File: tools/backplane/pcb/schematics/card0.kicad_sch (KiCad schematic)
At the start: 3 parts

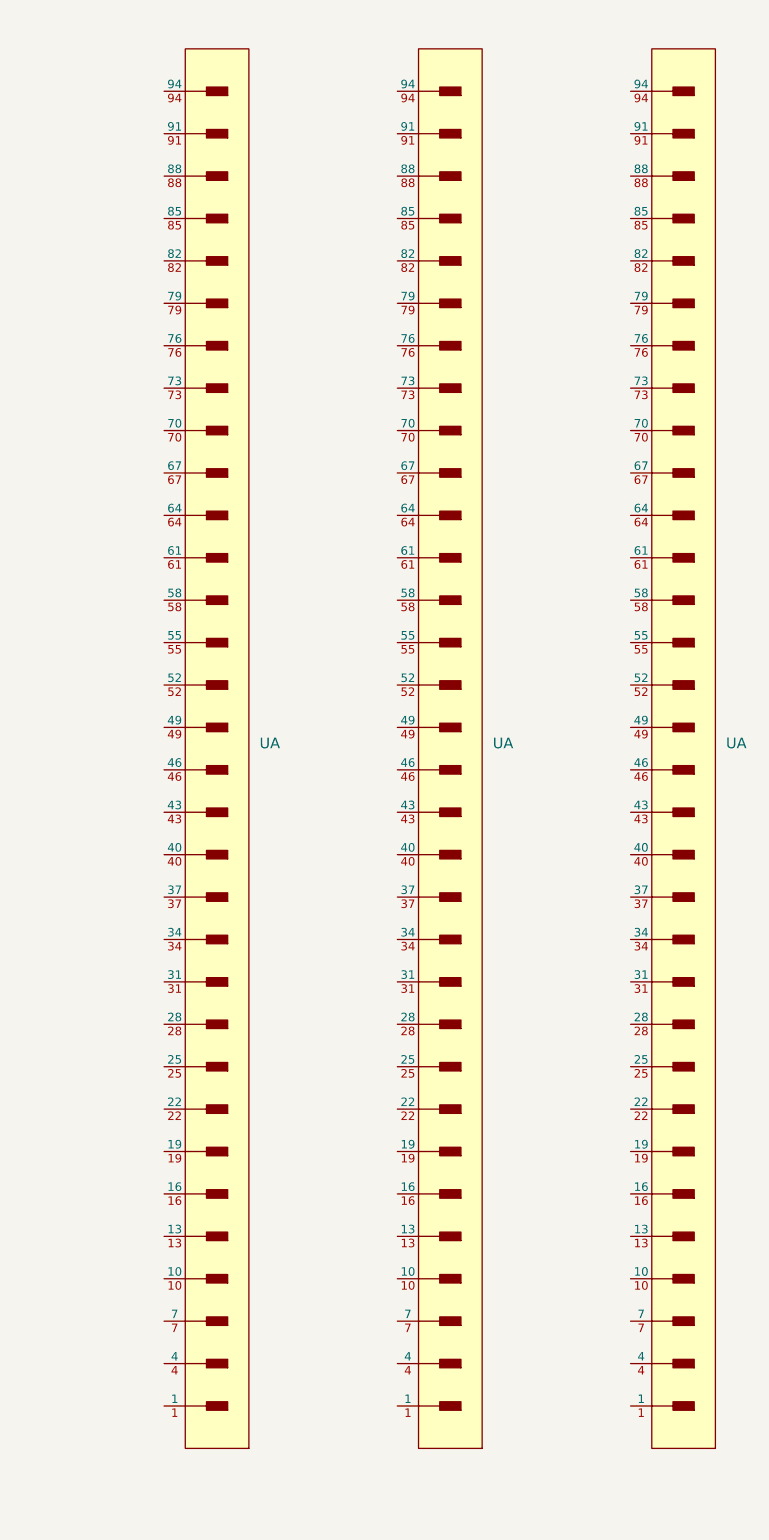
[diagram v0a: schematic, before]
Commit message: start routing the backplane
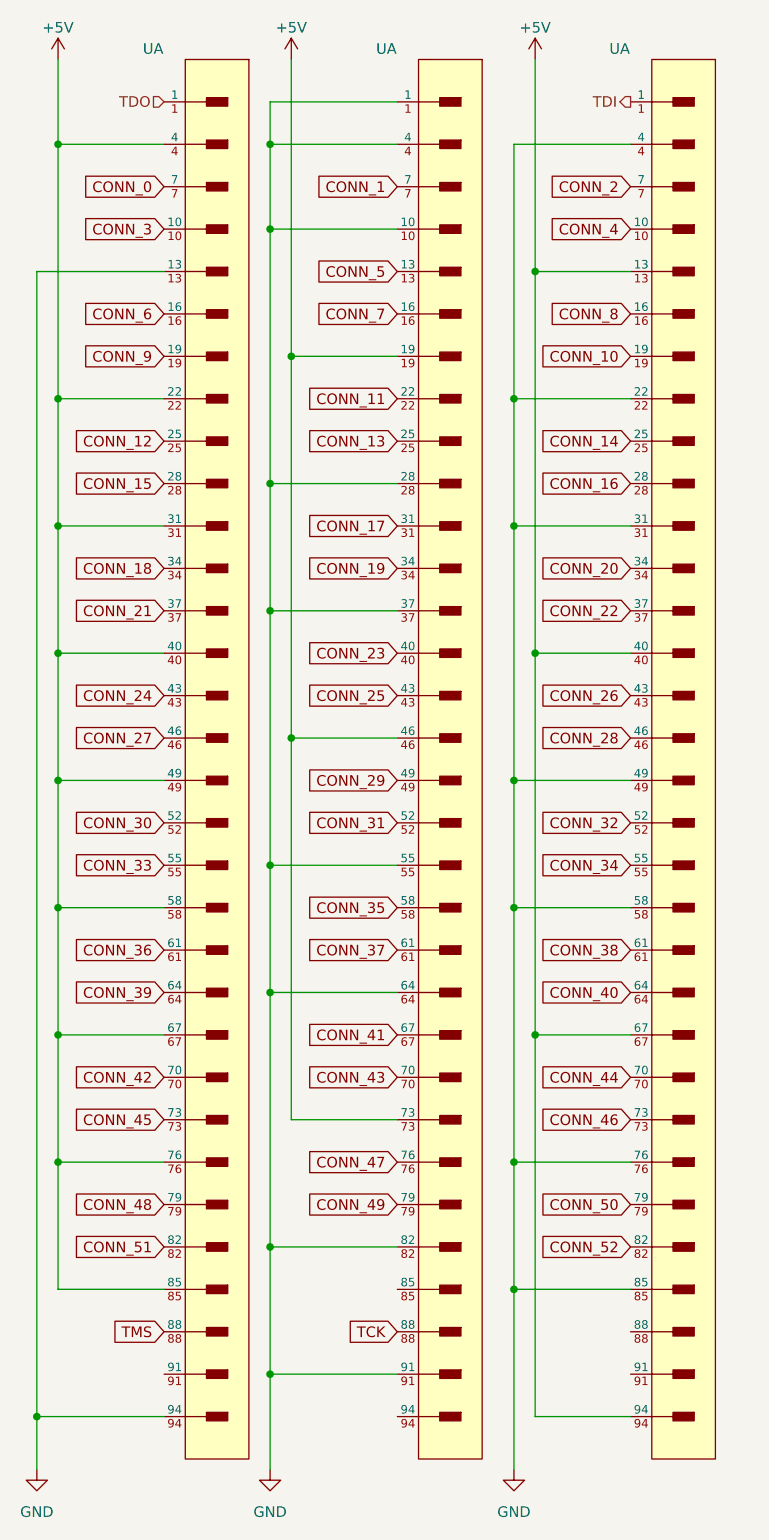
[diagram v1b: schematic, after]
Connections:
- net TDI: now reaches U.1
- net CONN_4: now reaches U.10
- net +5V: now reaches U.13
- net +5V: now also U.19, U.22, U.31, U.4, U.40, U.40, U.46, U.49, U.58, U.67, U.67, U.73, U.76, U.85, U.94
- net CONN_8: now reaches U.16
- net CONN_10: now reaches U.19
- net GND: now reaches U.22
- net GND: now also U.1, U.10, U.13, U.28, U.31, U.37, U.4, U.4, U.49, U.55, U.58, U.64, U.76, U.82, U.85, U.91, U.94
- net CONN_14: now reaches U.25
- net CONN_16: now reaches U.28
- net CONN_20: now reaches U.34
- net CONN_22: now reaches U.37
- net CONN_26: now reaches U.43
- net CONN_28: now reaches U.46
- net CONN_32: now reaches U.52
- net CONN_34: now reaches U.55
- net CONN_38: now reaches U.61
- net CONN_40: now reaches U.64
- net CONN_2: now reaches U.7
- net CONN_44: now reaches U.70
- net CONN_46: now reaches U.73
- net CONN_50: now reaches U.79
- net CONN_52: now reaches U.82
- net TDO: now reaches U.1
- net CONN_3: now reaches U.10
- net CONN_6: now reaches U.16
- net CONN_9: now reaches U.19
- net CONN_12: now reaches U.25
- net CONN_15: now reaches U.28
- net CONN_18: now reaches U.34
- net CONN_21: now reaches U.37
- net CONN_24: now reaches U.43
- net CONN_27: now reaches U.46
- net CONN_30: now reaches U.52
- net CONN_33: now reaches U.55
- net CONN_36: now reaches U.61
- net CONN_39: now reaches U.64
- net CONN_0: now reaches U.7
- net CONN_42: now reaches U.70
- net CONN_45: now reaches U.73
- net CONN_48: now reaches U.79
- net CONN_51: now reaches U.82
- net TMS: now reaches U.88
- net CONN_5: now reaches U.13
- net CONN_7: now reaches U.16
- net CONN_11: now reaches U.22
- net CONN_13: now reaches U.25
- net CONN_17: now reaches U.31
- net CONN_19: now reaches U.34
- net CONN_23: now reaches U.40
- net CONN_25: now reaches U.43
- net CONN_29: now reaches U.49
- net CONN_31: now reaches U.52
- net CONN_35: now reaches U.58
- net CONN_37: now reaches U.61
- net CONN_41: now reaches U.67
- net CONN_1: now reaches U.7
- net CONN_43: now reaches U.70
- net CONN_47: now reaches U.76
- net CONN_49: now reaches U.79
- net TCK: now reaches U.88
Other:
- moved on the sheet: UA
